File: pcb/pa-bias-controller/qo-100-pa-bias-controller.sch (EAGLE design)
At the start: 115 parts, among them CON1 3P-SH-SIDE, CON2 2EDG-5P-5MM, CON3 2EDG-5P-5MM, CON4 2EDG-2P-5MM, CON5 2P-SH-SIDE, CON6 2P-SH-SIDE, U1 EFM32TG11B120F128GM32, U2 MCP1501-25, U3 MAX11300, U4 MAX44285TAUA+, U5 MIC23155, U6 LT8636

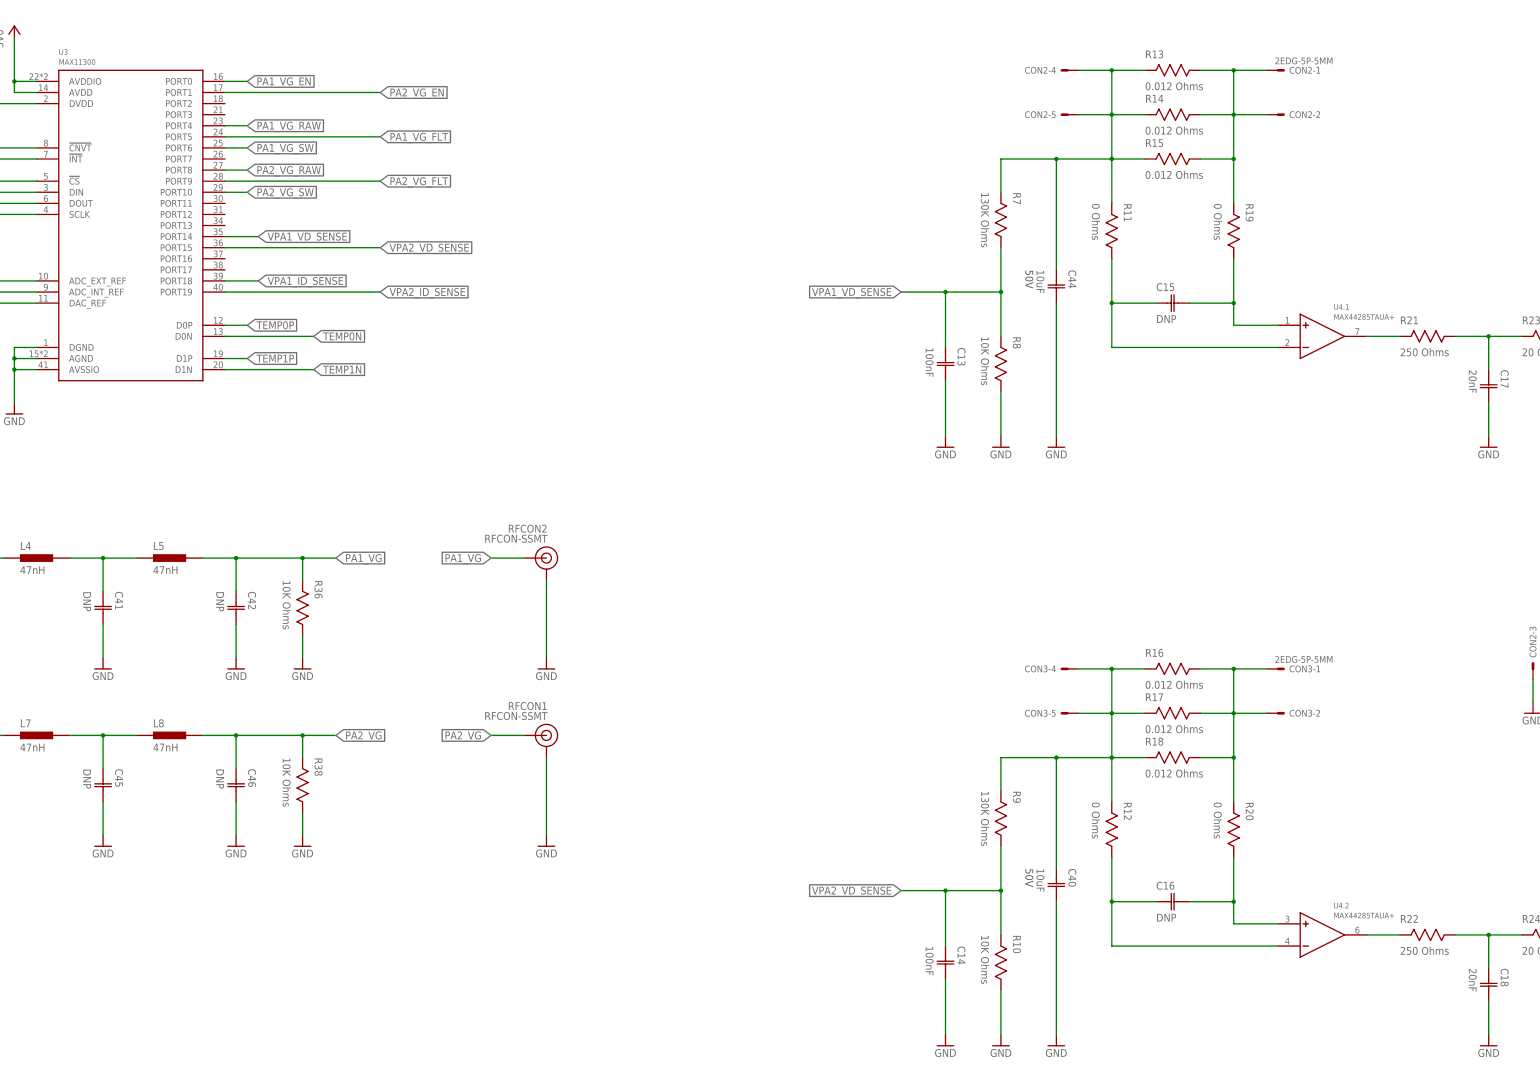
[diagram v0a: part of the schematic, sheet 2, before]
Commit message: PA Bias Controller assembly BOM changes
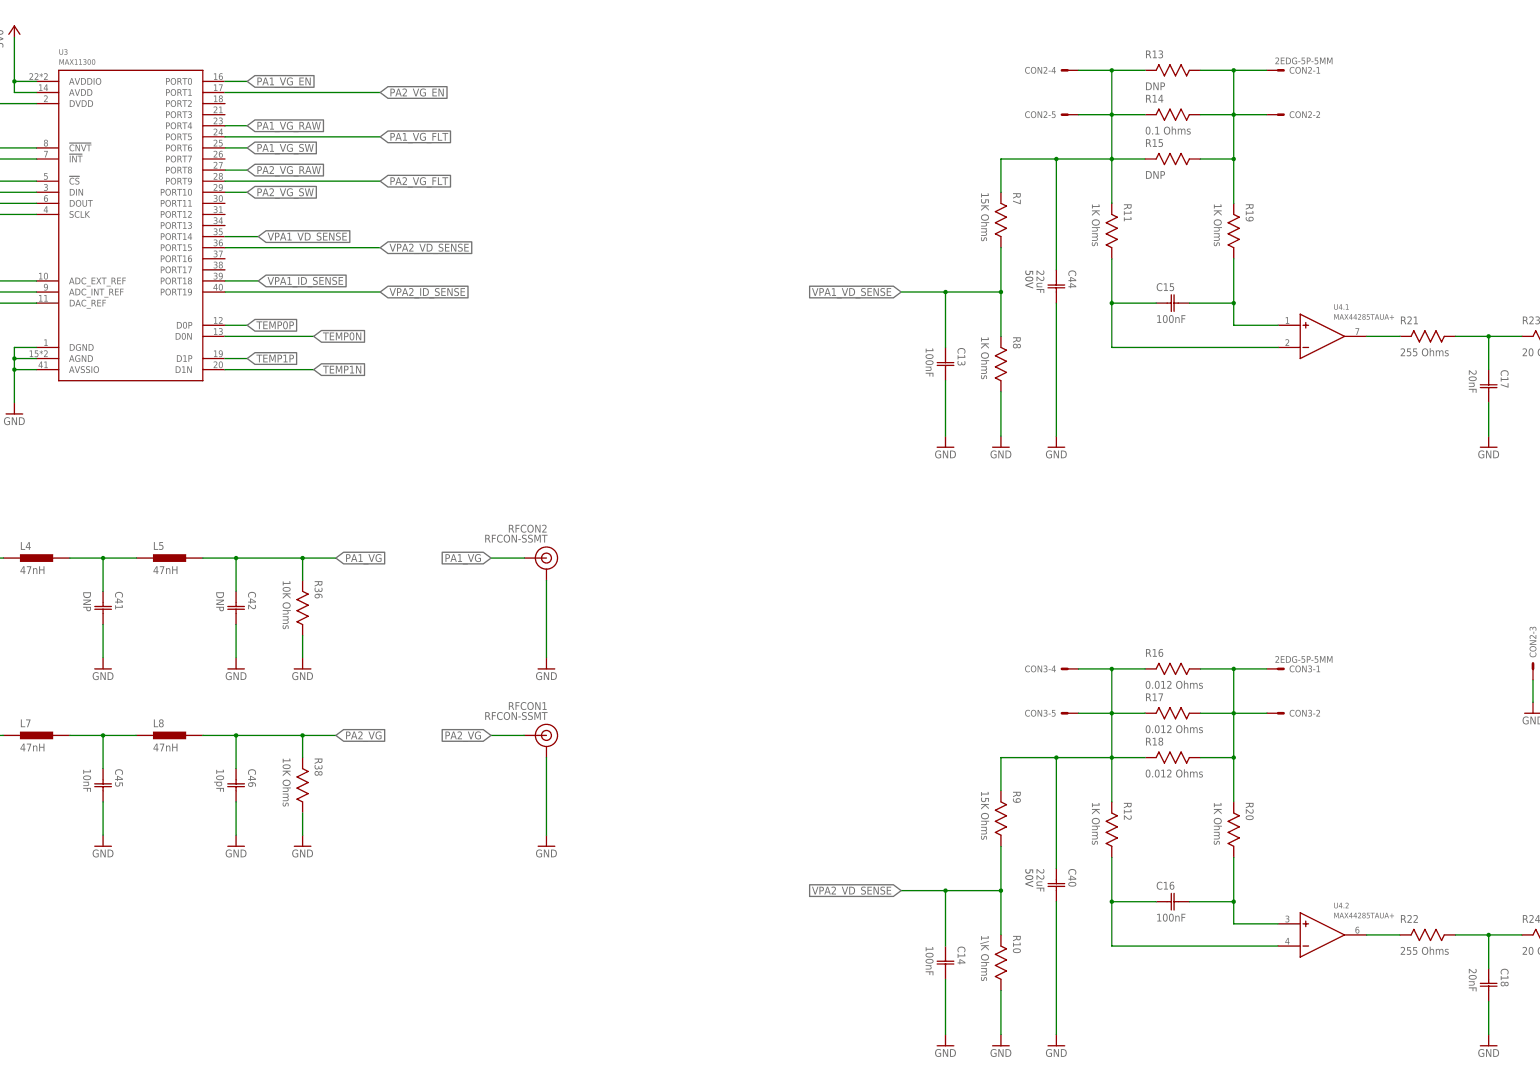
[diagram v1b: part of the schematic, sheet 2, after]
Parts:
- C15, C16: value DNP -> 100nF
- C40, C44: value 10uF -> 22uF
- C45: value DNP -> 10nF
- C46: value DNP -> 10pF
- R10: value 10K Ohms -> 1\K Ohms
- R11, R12, R19, R20: value 0 Ohms -> 1K Ohms
- R13, R15: value 0.012 Ohms -> DNP
- R14: value 0.012 Ohms -> 0.1 Ohms
- R2, R3: value 0 Ohms -> 100 Ohms
- R21, R22: value 250 Ohms -> 255 Ohms
- R7, R9: value 130K Ohms -> 15K Ohms
- R8: value 10K Ohms -> 1K Ohms
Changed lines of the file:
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@@
 </classes>
 <parts>
-<part name="R13" library="Resistor" deviceset="RESISTOR" device="-2512" value="0.012 Ohms"/>
-<part name="R14" library="Resistor" deviceset="RESISTOR" device="-2512" value="0.012 Ohms"/>
-<part name="R15" library="Resistor" deviceset="RESISTOR" device="-2512" value="0.012 Ohms"/>
+<part name="R13" library="Resistor" deviceset="RESISTOR" device="-2512" value="DNP"/>
+<part name="R14" library="Resistor" deviceset="RESISTOR" device="-2512" value="0.1 Ohms"/>
+<part name="R15" library="Resistor" deviceset="RESISTOR" device="-2512" value="DNP"/>
 <part name="CON2" library="Generic Connector" deviceset="2EDG-5P" device="-5MM"/>
 <part name="GND2" library="Supply Symbol" deviceset="GND" device=""/>
@@
 <part name="CON1" library="JST" deviceset="3P" device="-SH-SIDE" value="3P-SH-SIDE"/>
 <part name="GND24" library="Supply Symbol" deviceset="GND" device=""/>
-<part name="R2" library="Resistor" deviceset="RESISTOR" device="-0603" value="0 Ohms"/>
-<part name="R3" library="Resistor" deviceset="RESISTOR" device="-0603" value="0 Ohms"/>
+<part name="R2" library="Resistor" deviceset="RESISTOR" device="-0603" value="100 Ohms"/>
+<part name="R3" library="Resistor" deviceset="RESISTOR" device="-0603" value="100 Ohms"/>
 <part name="C3" library="Capacitor" deviceset="CAPACITOR" device="-0603" value="100nF"/>
 <part name="GND26" library="Supply Symbol" deviceset="GND" device=""/>
@@
 </part>
 <part name="GND1027" library="Supply Symbol" deviceset="GND" device=""/>
-<part name="C15" library="Capacitor" deviceset="CAPACITOR" device="-0603" value="DNP"/>
-<part name="R19" library="Resistor" deviceset="RESISTOR" device="-0603" value="0 Ohms"/>
-<part name="R11" library="Resistor" deviceset="RESISTOR" device="-0603" value="0 Ohms"/>
+<part name="C15" library="Capacitor" deviceset="CAPACITOR" device="-0603" value="100nF"/>
+<part name="R19" library="Resistor" deviceset="RESISTOR" device="-0603" value="1K Ohms"/>
+<part name="R11" library="Resistor" deviceset="RESISTOR" device="-0603" value="1K Ohms"/>
 <part name="R23" library="Resistor" deviceset="RESISTOR" device="-0603" value="20 Ohms"/>
 <part name="C19" library="Capacitor" deviceset="CAPACITOR" device="-0603" value="220nF"/>
@@
 <part name="5V00002" library="Supply Symbol" deviceset="5V0" device=""/>
 <part name="3V2" library="Supply Symbol" deviceset="3V3" device=""/>
-<part name="R7" library="Resistor" deviceset="RESISTOR" device="-0603" value="130K Ohms"/>
-<part name="R8" library="Resistor" deviceset="RESISTOR" device="-0603" value="10K Ohms"/>
+<part name="R7" library="Resistor" deviceset="RESISTOR" device="-0603" value="15K Ohms"/>
+<part name="R8" library="Resistor" deviceset="RESISTOR" device="-0603" value="1K Ohms"/>
 <part name="GND3" library="Supply Symbol" deviceset="GND" device=""/>
 <part name="C13" library="Capacitor" deviceset="CAPACITOR" device="-0603" value="100nF"/>
@@
 <part name="R18" library="Resistor" deviceset="RESISTOR" device="-2512" value="0.012 Ohms"/>
 <part name="CON3" library="Generic Connector" deviceset="2EDG-5P" device="-5MM"/>
-<part name="C16" library="Capacitor" deviceset="CAPACITOR" device="-0603" value="DNP"/>
-<part name="R20" library="Resistor" deviceset="RESISTOR" device="-0603" value="0 Ohms"/>
-<part name="R12" library="Resistor" deviceset="RESISTOR" device="-0603" value="0 Ohms"/>
+<part name="C16" library="Capacitor" deviceset="CAPACITOR" device="-0603" value="100nF"/>
+<part name="R20" library="Resistor" deviceset="RESISTOR" device="-0603" value="1K Ohms"/>
+<part name="R12" library="Resistor" deviceset="RESISTOR" device="-0603" value="1K Ohms"/>
 <part name="R24" library="Resistor" deviceset="RESISTOR" device="-0603" value="20 Ohms"/>
 <part name="C20" library="Capacitor" deviceset="CAPACITOR" device="-0603" value="220nF"/>
 <part name="GND6" library="Supply Symbol" deviceset="GND" device=""/>
-<part name="R9" library="Resistor" deviceset="RESISTOR" device="-0603" value="130K Ohms"/>
-<part name="R10" library="Resistor" deviceset="RESISTOR" device="-0603" value="10K Ohms"/>
+<part name="R9" library="Resistor" deviceset="RESISTOR" device="-0603" value="15K Ohms"/>
+<part name="R10" library="Resistor" deviceset="RESISTOR" device="-0603" value="1\K Ohms"/>
 <part name="GND7" library="Supply Symbol" deviceset="GND" device=""/>
 <part name="C14" library="Capacitor" deviceset="CAPACITOR" device="-0603" value="100nF"/>
@@
 <part name="GND9" library="Supply Symbol" deviceset="GND" device=""/>
 <part name="GND10" library="Supply Symbol" deviceset="GND" device=""/>
-<part name="R22" library="Resistor" deviceset="RESISTOR" device="-0603" value="250 Ohms"/>
+<part name="R22" library="Resistor" deviceset="RESISTOR" device="-0603" value="255 Ohms"/>
 <part name="C18" library="Capacitor" deviceset="CAPACITOR" device="-0603" value="20nF"/>
 <part name="GND11" library="Supply Symbol" deviceset="GND" device=""/>
-<part name="R21" library="Resistor" deviceset="RESISTOR" device="-0603" value="250 Ohms"/>
+<part name="R21" library="Resistor" deviceset="RESISTOR" device="-0603" value="255 Ohms"/>
 <part name="C17" library="Capacitor" deviceset="CAPACITOR" device="-0603" value="20nF"/>
 <part name="GND12" library="Supply Symbol" deviceset="GND" device=""/>
@@
 <part name="L7" library="Inductor" deviceset="INDUCTOR" device="-0603" value="47nH"/>
 <part name="L8" library="Inductor" deviceset="INDUCTOR" device="-0603" value="47nH"/>
-<part name="C45" library="Capacitor" deviceset="CAPACITOR" device="-0603" value="DNP"/>
+<part name="C45" library="Capacitor" deviceset="CAPACITOR" device="-0603" value="10nF"/>
 <part name="GND32" library="Supply Symbol" deviceset="GND" device=""/>
-<part name="C46" library="Capacitor" deviceset="CAPACITOR" device="-0603" value="DNP"/>
+<part name="C46" library="Capacitor" deviceset="CAPACITOR" device="-0603" value="10pF"/>
 <part name="GND33" library="Supply Symbol" deviceset="GND" device=""/>
 <part name="GND34" library="Supply Symbol" deviceset="GND" device=""/>
@@
 <part name="R40" library="Resistor" deviceset="RESISTOR" device="-0603" value="1K Ohms"/>
 <part name="3V14" library="Supply Symbol" deviceset="3V3" device=""/>
-<part name="C40" library="Capacitor" deviceset="CAPACITOR" device="-2220" value="10uF">
+<part name="C40" library="Capacitor" deviceset="CAPACITOR" device="-2220" value="22uF">
 <attribute name="VOLTAGE" value="50V"/>
 </part>
 <part name="GND35" library="Supply Symbol" deviceset="GND" device=""/>
-<part name="C44" library="Capacitor" deviceset="CAPACITOR" device="-2220" value="10uF">
-<attribute name="VOLTAGE" value="50V"/>
-</part>
+<part name="C44" library="Capacitor" deviceset="CAPACITOR" device="-2220" value="22uF">
+<attribute name="VOLTAGE" value="50V"/>
+</part>

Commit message: Update I2C slave resistors to minimize load effect when powered down
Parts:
- R2, R3: value 100 Ohms -> 1K Ohms
- R39, R40: value 1K Ohms -> 47K Ohms
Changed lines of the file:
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@@
 <part name="CON1" library="JST" deviceset="3P" device="-SH-SIDE" value="3P-SH-SIDE"/>
 <part name="GND24" library="Supply Symbol" deviceset="GND" device=""/>
-<part name="R2" library="Resistor" deviceset="RESISTOR" device="-0603" value="100 Ohms"/>
-<part name="R3" library="Resistor" deviceset="RESISTOR" device="-0603" value="100 Ohms"/>
+<part name="R2" library="Resistor" deviceset="RESISTOR" device="-0603" value="1K Ohms"/>
+<part name="R3" library="Resistor" deviceset="RESISTOR" device="-0603" value="1K Ohms"/>
 <part name="C3" library="Capacitor" deviceset="CAPACITOR" device="-0603" value="100nF"/>
 <part name="GND26" library="Supply Symbol" deviceset="GND" device=""/>
@@
 </part>
 <part name="U1" library="EFM32" deviceset="EFM32TG11B1*M32" device="" technology="20F128G"/>
-<part name="R39" library="Resistor" deviceset="RESISTOR" device="-0603" value="1K Ohms"/>
+<part name="R39" library="Resistor" deviceset="RESISTOR" device="-0603" value="47K Ohms"/>
 <part name="3V13" library="Supply Symbol" deviceset="3V3" device=""/>
-<part name="R40" library="Resistor" deviceset="RESISTOR" device="-0603" value="1K Ohms"/>
+<part name="R40" library="Resistor" deviceset="RESISTOR" device="-0603" value="47K Ohms"/>
 <part name="3V14" library="Supply Symbol" deviceset="3V3" device=""/>
 <part name="C40" library="Capacitor" deviceset="CAPACITOR" device="-2220" value="22uF">

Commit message: Revert I2C resistor chnges because they do not work
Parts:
- R2, R3: value 1K Ohms -> 100 Ohms
- R39, R40: value 47K Ohms -> 1K Ohms
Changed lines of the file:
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@@
 <part name="CON1" library="JST" deviceset="3P" device="-SH-SIDE" value="3P-SH-SIDE"/>
 <part name="GND24" library="Supply Symbol" deviceset="GND" device=""/>
-<part name="R2" library="Resistor" deviceset="RESISTOR" device="-0603" value="1K Ohms"/>
-<part name="R3" library="Resistor" deviceset="RESISTOR" device="-0603" value="1K Ohms"/>
+<part name="R2" library="Resistor" deviceset="RESISTOR" device="-0603" value="100 Ohms"/>
+<part name="R3" library="Resistor" deviceset="RESISTOR" device="-0603" value="100 Ohms"/>
 <part name="C3" library="Capacitor" deviceset="CAPACITOR" device="-0603" value="100nF"/>
 <part name="GND26" library="Supply Symbol" deviceset="GND" device=""/>
@@
 </part>
 <part name="U1" library="EFM32" deviceset="EFM32TG11B1*M32" device="" technology="20F128G"/>
-<part name="R39" library="Resistor" deviceset="RESISTOR" device="-0603" value="47K Ohms"/>
+<part name="R39" library="Resistor" deviceset="RESISTOR" device="-0603" value="1K Ohms"/>
 <part name="3V13" library="Supply Symbol" deviceset="3V3" device=""/>
-<part name="R40" library="Resistor" deviceset="RESISTOR" device="-0603" value="47K Ohms"/>
+<part name="R40" library="Resistor" deviceset="RESISTOR" device="-0603" value="1K Ohms"/>
 <part name="3V14" library="Supply Symbol" deviceset="3V3" device=""/>
 <part name="C40" library="Capacitor" deviceset="CAPACITOR" device="-2220" value="22uF">
